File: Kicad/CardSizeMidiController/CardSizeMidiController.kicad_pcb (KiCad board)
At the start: 2 copper layers, 85.7 x 54 mm, 41 parts, among them J1 USB_B, J2 Conn_02x03_Odd_Even, J3 MIDI_OUT, J4 AudioJack3, J5 Screw_Terminal_01x01, J6 Screw_Terminal_01x01, J7 Screw_Terminal_01x01, J8 Screw_Terminal_01x01, SW0 SW_Push, SW1 SW_Push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

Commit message: pcb layout changes
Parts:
- J3: value MIDI_OUT -> MIDI OUT
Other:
- board text added: "1"
- board text added: "ICSP"

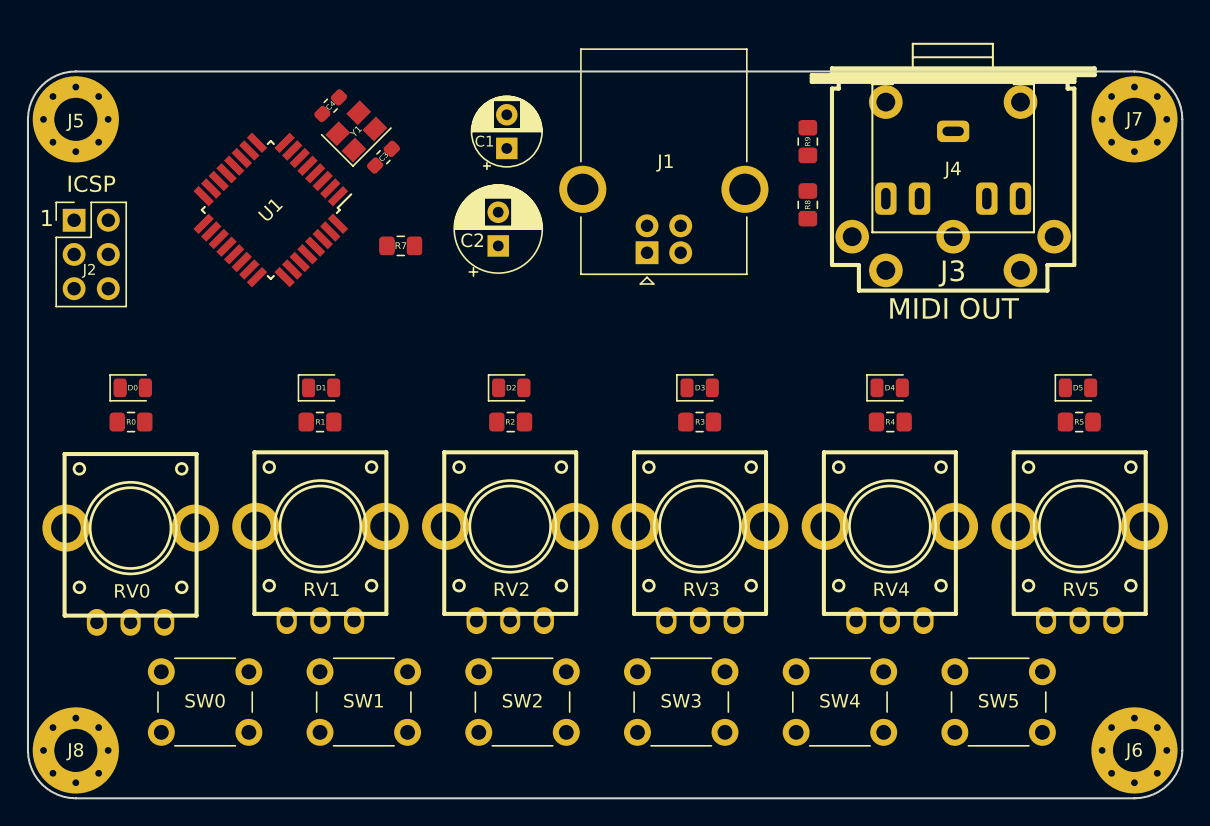
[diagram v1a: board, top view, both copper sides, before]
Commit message: Update CardSizeMidiController.kicad_pcb
silkscreen changes
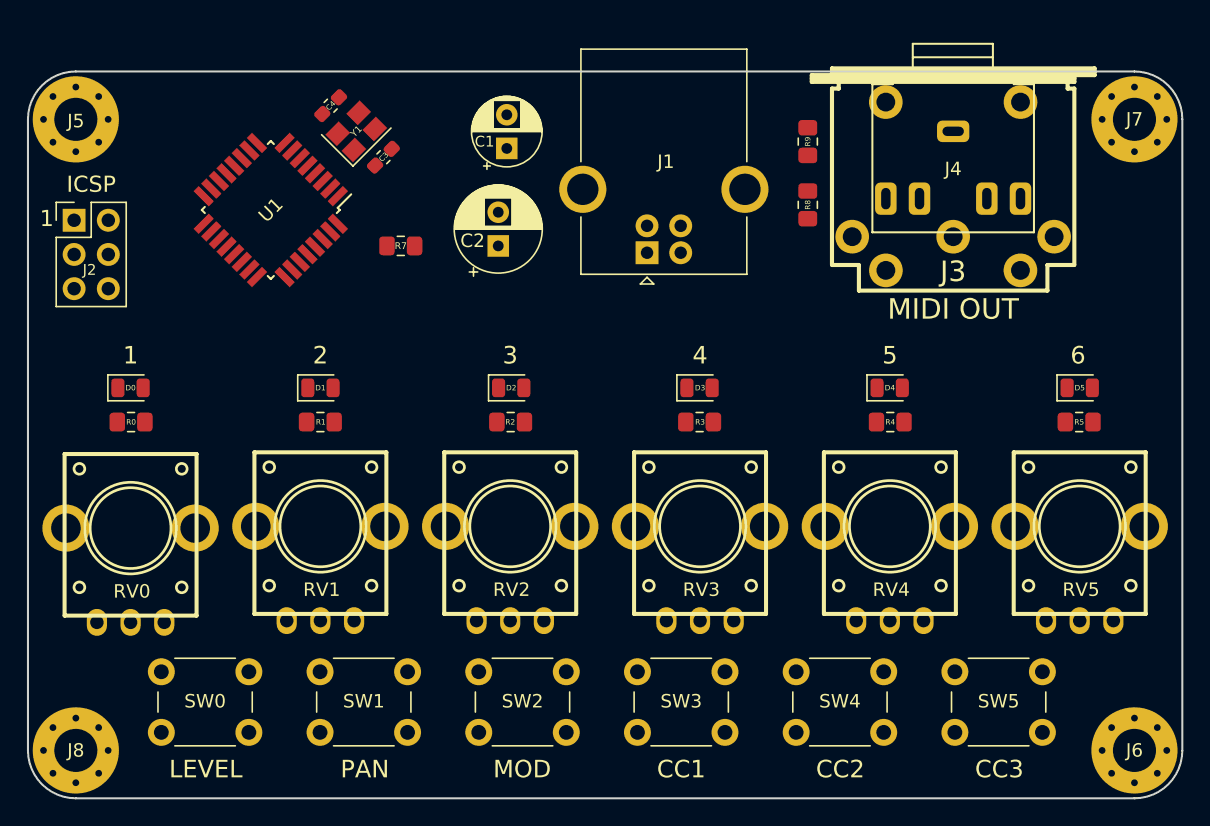
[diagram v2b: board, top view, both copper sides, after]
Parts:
- moved D0 0.17 mm to (7.62, 23.5)
- moved D5 0.13 mm to (78.1, 23.5)
- moved D1 0.06 mm to (21.7, 23.5)
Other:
- board text added: "2"
- board text added: "3"
- board text added: "4"
- board text added: "5"
- board text added: "6"
- board text added: "CC1"
- board text added: "CC2"
- board text added: "CC3"
- board text added: "JLCJLCJLCJLC"
- board text added: "LEVEL"
- board text added: "MOD"
- board text added: "PAN"
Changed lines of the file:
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@@
   (general
     (thickness 1.6)
-    (drawings 10)
+    (drawings 23)
     (tracks 0)
     (zones 0)
@@
   )
   (module LED_SMD:LED_0805_2012Metric (layer F.Cu)
-    (at 7.785857 23.495)
+    (at 7.62 23.495)
     (descr "LED SMD 0805 (2012 Metric), square (rectangular) end terminal, IPC_7351 nominal, (Body size source: https://docs.google.com/spreadsheets/d/1BsfQQcO9C6DZCsRaXUlFlo91Tg2WpOkGARC1WS5S8t0/edit?usp=sharing), generated with kicad-footprint-generator")
     (tags diode)
@@
   )
   (module LED_SMD:LED_0805_2012Metric (layer F.Cu)
-    (at 21.773714 23.495)
+    (at 21.717 23.495)
     (descr "LED SMD 0805 (2012 Metric), square (rectangular) end terminal, IPC_7351 nominal, (Body size source: https://docs.google.com/spreadsheets/d/1BsfQQcO9C6DZCsRaXUlFlo91Tg2WpOkGARC1WS5S8t0/edit?usp=sharing), generated with kicad-footprint-generator")
     (tags diode)
@@
   )
   (module LED_SMD:LED_0805_2012Metric (layer F.Cu)
-    (at 77.979142 23.495)
+    (at 78.105 23.495)
     (descr "LED SMD 0805 (2012 Metric), square (rectangular) end terminal, IPC_7351 nominal, (Body size source: https://docs.google.com/spreadsheets/d/1BsfQQcO9C6DZCsRaXUlFlo91Tg2WpOkGARC1WS5S8t0/edit?usp=sharing), generated with kicad-footprint-generator")
     (tags diode)
@@
   )
   (module Resistor_SMD:R_0805_2012Metric_Pad1.15x1.40mm_HandSolder (layer F.Cu)
-    (at 21.689428 26.035)
+    (at 21.717 26.035)
     (descr "Resistor SMD 0805 (2012 Metric), square (rectangular) end terminal, IPC_7351 nominal with elongated pad for handsoldering. (Body size source: https://docs.google.com/spreadsheets/d/1BsfQQcO9C6DZCsRaXUlFlo91Tg2WpOkGARC1WS5S8t0/edit?usp=sharing), generated with kicad-footprint-generator")
     (tags "resistor handsolder")
@@
     )
   )
+  (gr_text 6 (at 77.978 21.082) (layer F.SilkS)
+    (effects (font (size 1.3 1.3) (thickness 0.3)))
+  )
+  (gr_text 5 (at 64.008 21.082) (layer F.SilkS)
+    (effects (font (size 1.3 1.3) (thickness 0.3)))
+  )
+  (gr_text 4 (at 49.911 21.082) (layer F.SilkS)
+    (effects (font (size 1.3 1.3) (thickness 0.3)))
+  )
+  (gr_text 3 (at 35.814 21.082) (layer F.SilkS)
+    (effects (font (size 1.3 1.3) (thickness 0.3)))
+  )
+  (gr_text 2 (at 21.717 21.082) (layer F.SilkS)
+    (effects (font (size 1.3 1.3) (thickness 0.3)))
+  )
+  (gr_text 1 (at 7.62 21.082) (layer F.SilkS)
+    (effects (font (size 1.3 1.3) (thickness 0.3)))
+  )
+  (gr_text JLCJLCJLCJLC (at 1.369 41.425 90) (layer B.SilkS)
+    (effects (font (size 1 1) (thickness 0.2)) (justify mirror))
+  )
+  (gr_text MOD (at 36.703 51.816) (layer F.SilkS)
+    (effects (font (size 1.3 1.3) (thickness 0.3)))
+  )
+  (gr_text "CC2\n" (at 60.325 51.816) (layer F.SilkS)
+    (effects (font (size 1.3 1.3) (thickness 0.3)))
+  )
+  (gr_text CC1 (at 48.514 51.816) (layer F.SilkS)
+    (effects (font (size 1.3 1.3) (thickness 0.3)))
+  )
+  (gr_text LEVEL (at 13.208 51.816) (layer F.SilkS)
+    (effects (font (size 1.3 1.3) (thickness 0.3)))
+  )
+  (gr_text PAN (at 25.019 51.816) (layer F.SilkS)
+    (effects (font (size 1.3 1.3) (thickness 0.3)))
+  )
+  (gr_text CC3 (at 72.136 51.816) (layer F.SilkS)
+    (effects (font (size 1.3 1.3) (thickness 0.3)))
+  )
   (gr_text 1 (at 1.397 10.922) (layer F.SilkS)

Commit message: layout adjustments
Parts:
- moved J4 2.03 mm to (68.7, 6.48)
- moved J1 1.65 mm to (46.0, 15.1)
- moved R8 1.65 mm to (57.9, 11.6)
- moved R9 1.65 mm to (57.9, 6.86)
- moved SW5 0.51 mm to (69.3, 44.6)
- moved SW4 0.41 mm to (57.5, 44.6)
- moved SW3 0.30 mm to (45.6, 44.6)
- moved J3 0.25 mm to (68.7, 9.53)
- moved SW2 0.20 mm to (33.7, 44.6)
- moved SW1 0.10 mm to (21.8, 44.6)
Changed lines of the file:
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@@
   )
   (module Button_Switch_THT:SW_PUSH_6mm_H5mm (layer F.Cu)
-    (at 68.834 44.577)
+    (at 69.342 44.577)
     (descr "tactile push button, 6x6mm e.g. PHAP33xx series, height=5mm")
     (tags "tact sw push 6mm")
@@
   )
   (module Button_Switch_THT:SW_PUSH_6mm_H5mm (layer F.Cu)
-    (at 57.0484 44.577)
+    (at 57.4548 44.577)
     (descr "tactile push button, 6x6mm e.g. PHAP33xx series, height=5mm")
     (tags "tact sw push 6mm")
@@
   )
   (module Button_Switch_THT:SW_PUSH_6mm_H5mm (layer F.Cu)
-    (at 45.2628 44.577)
+    (at 45.5676 44.577)
     (descr "tactile push button, 6x6mm e.g. PHAP33xx series, height=5mm")
     (tags "tact sw push 6mm")
@@
   )
   (module Button_Switch_THT:SW_PUSH_6mm_H5mm (layer F.Cu)
-    (at 33.4772 44.577)
+    (at 33.6804 44.577)
     (descr "tactile push button, 6x6mm e.g. PHAP33xx series, height=5mm")
     (tags "tact sw push 6mm")
@@
   )
   (module Button_Switch_THT:SW_PUSH_6mm_H5mm (layer F.Cu)
-    (at 21.6916 44.577)
+    (at 21.7932 44.577)
     (descr "tactile push button, 6x6mm e.g. PHAP33xx series, height=5mm")
     (tags "tact sw push 6mm")
@@
   )
   (module Connector_USB:USB_B_OST_USB-B1HSxx_Horizontal (layer F.Cu)
-    (at 45.974 13.462 90)
+    (at 45.974 15.113 90)
     (descr "USB B receptacle, Horizontal, through-hole, http://www.on-shore.com/wp-content/uploads/2015/09/usb-b1hsxx.pdf")
     (tags "USB-B receptacle horizontal through-hole")
@@
   )
   (module Resistor_SMD:R_0805_2012Metric_Pad1.15x1.40mm_HandSolder (layer F.Cu)
-    (at 57.912 5.207 270)
+    (at 57.912 6.858 270)
     (descr "Resistor SMD 0805 (2012 Metric), square (rectangular) end terminal, IPC_7351 nominal with elongated pad for handsoldering. (Body size source: https://docs.google.com/spreadsheets/d/1BsfQQcO9C6DZCsRaXUlFlo91Tg2WpOkGARC1WS5S8t0/edit?usp=sharing), generated with kicad-footprint-generator")
     (tags "resistor handsolder")
@@
   )
   (module Resistor_SMD:R_0805_2012Metric_Pad1.15x1.40mm_HandSolder (layer F.Cu)
-    (at 57.912 9.906 90)
+    (at 57.912 11.557 90)
     (descr "Resistor SMD 0805 (2012 Metric), square (rectangular) end terminal, IPC_7351 nominal with elongated pad for handsoldering. (Body size source: https://docs.google.com/spreadsheets/d/1BsfQQcO9C6DZCsRaXUlFlo91Tg2WpOkGARC1WS5S8t0/edit?usp=sharing), generated with kicad-footprint-generator")
     (tags "resistor handsolder")
@@
   )
   (module "SensaiLib:Jack stereo tayda" (layer F.Cu)
-    (at 68.707 4.445 180)
+    (at 68.707 6.477 180)
     (fp_text reference J4 (at 0 -2.794 180) (layer F.SilkS)
       (effects (font (size 1 1) (thickness 0.15)))
@@
   )
   (module SensaiLib:din-5 (layer F.Cu)
-    (at 68.707 9.271 180)
+    (at 68.707 9.525 180)
     (descr "Din 5 (MIDI), Pro Signal P/N PSG03463")
     (fp_text reference J3 (at 0 -5.588 180) (layer F.SilkS)
@@
     (effects (font (size 1 1) (thickness 0.2)) (justify mirror))
   )
-  (gr_text MOD (at 36.703 51.816) (layer F.SilkS)
+  (gr_text MOD (at 36.957 51.816) (layer F.SilkS)
     (effects (font (size 1.3 1.3) (thickness 0.3)))
   )
-  (gr_text "CC2\n" (at 60.325 51.816) (layer F.SilkS)
+  (gr_text "CC2\n" (at 60.706 51.816) (layer F.SilkS)
     (effects (font (size 1.3 1.3) (thickness 0.3)))
   )
-  (gr_text CC1 (at 48.514 51.816) (layer F.SilkS)
+  (gr_text CC1 (at 48.768 51.816) (layer F.SilkS)
     (effects (font (size 1.3 1.3) (thickness 0.3)))
   )
@@
     (effects (font (size 1.3 1.3) (thickness 0.3)))
   )
-  (gr_text CC3 (at 72.136 51.816) (layer F.SilkS)
+  (gr_text CC3 (at 72.644 51.816) (layer F.SilkS)
     (effects (font (size 1.3 1.3) (thickness 0.3)))
   )

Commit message: Autorouted
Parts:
- moved C4 1.65 mm to (24.1, 2.54)
- moved Y1 1.65 mm to (26.0, 4.45)
- moved C3 1.65 mm to (28.1, 6.37)
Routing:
- net +5V: track 0.00 -> 188.3 mm, vias 0 -> 1
- net SCK: track 0.00 -> 121.1 mm
- net LED5: track 0.00 -> 106.6 mm, vias 0 -> 1
- net MISO: track 0.00 -> 95.1 mm, vias 0 -> 1
- net GND: track 0.00 -> 87.7 mm, vias 0 -> 1
- net A5: track 0.00 -> 79.1 mm
- net SW3: track 0.00 -> 67.3 mm, vias 0 -> 1
- net LED4: track 0.00 -> 58.0 mm, vias 0 -> 2
- net SW2: track 0.00 -> 57.5 mm, vias 0 -> 1
- net A4: track 0.00 -> 55.8 mm
- net LED1: track 0.00 -> 51.0 mm
- net SW1: track 0.00 -> 45.5 mm, vias 0 -> 1
- net LED3: track 0.00 -> 45.2 mm, vias 0 -> 2
- net SW0: track 0.00 -> 43.8 mm, vias 0 -> 1
- net TX: track 0.00 -> 42.7 mm
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- added copper zone on B.Cu, net GND
- added copper zone on F.Cu, net GND

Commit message: layout modifications
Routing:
- net A4: track 55.8 -> 55.2 mm
- net LED5: track 106.6 -> 106.1 mm
- net XTAL1: track 11.1 -> 10.6 mm
- net LED2: track 30.5 -> 30.0 mm
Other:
- board text added: "AUTHORIZED SIGNATURE"
- board text added: "JLC Order Number"
- board text added: "Version 0.2"
- board text added: "https://github.com/sensai7"
